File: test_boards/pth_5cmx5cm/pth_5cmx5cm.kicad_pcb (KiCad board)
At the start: 2 copper layers, 49.5 x 49.5 mm, 4 parts, among them Q1 BC560, Q2 2N3904

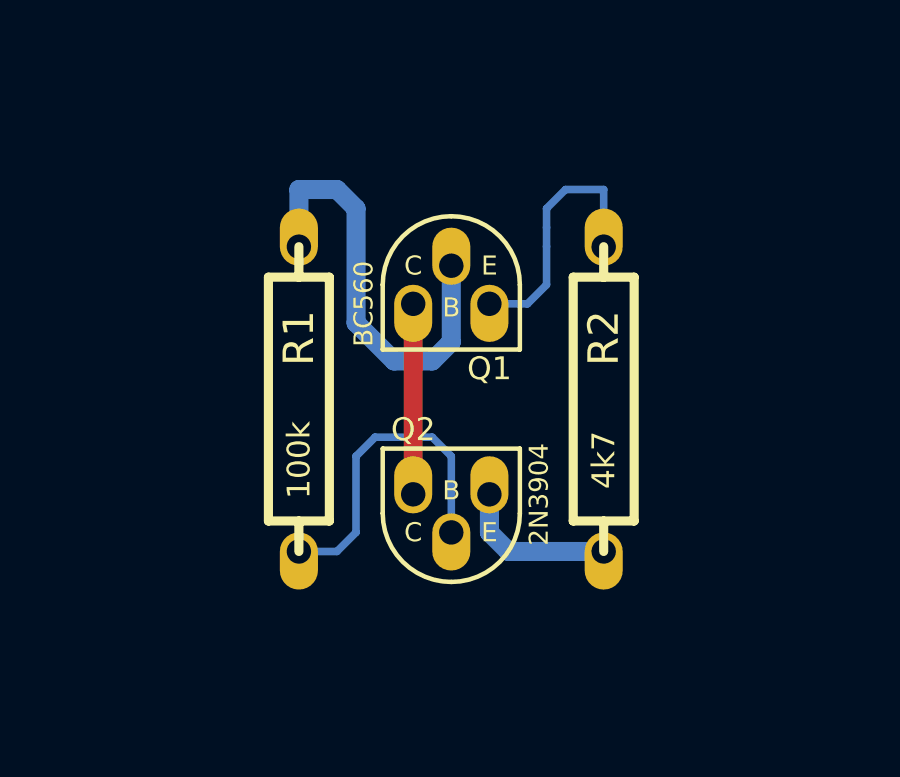
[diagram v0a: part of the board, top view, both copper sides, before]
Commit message: updating test board.
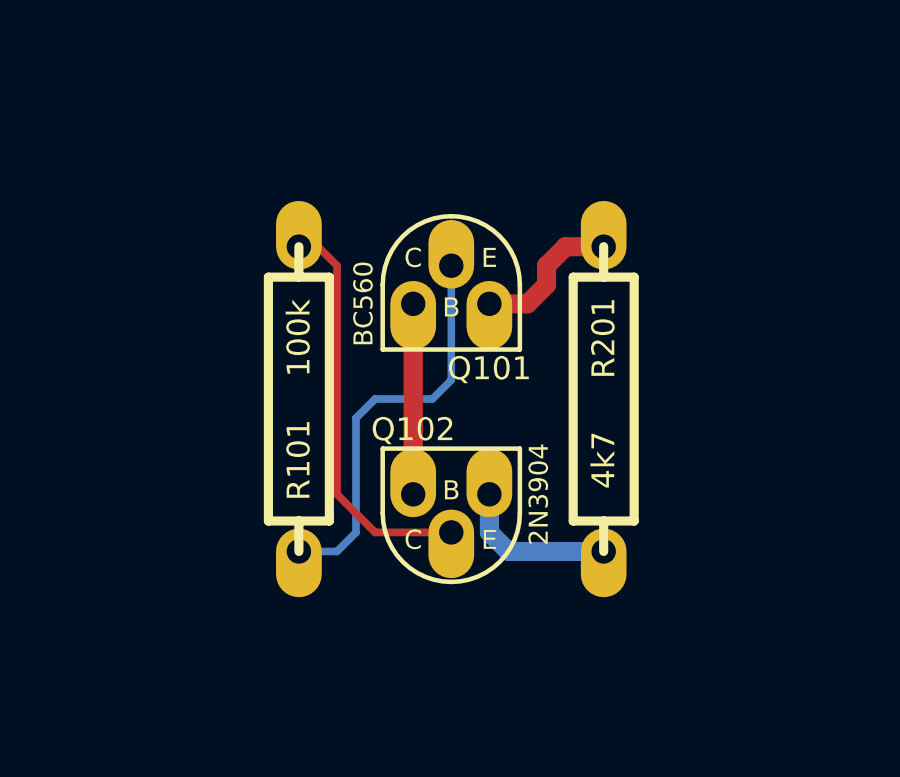
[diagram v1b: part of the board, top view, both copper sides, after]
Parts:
- removed Q1: BC560, TO-92_CBE
- removed Q2: 2N3904, TO-92_EBC
- removed R1: 100k, R_AXIAL_0W25
- removed R2: 4k7, R_AXIAL_0W25
- added Q101: BC560, TO-92_Q_CBE, F.Cu at (215.3, 118.7)
- added Q102: 2N3904, TO-92_Q_EBC, F.Cu at (215.3, 126.4)
- added R101: 100k, R_AXIAL_0W25, F.Cu at (210.2, 122.6)
- added R201: 4k7, R_AXIAL_0W25, F.Cu at (220.3, 122.6)
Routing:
- net N-000001: track 14.4 -> 4.97 mm
- net N-000002: track 5.34 -> 13.5 mm
- net N-000004: track 6.35 -> 13.5 mm
- net N-000005: track 10.9 -> 5.34 mm
- net N-000003: track 8.78 -> 6.35 mm

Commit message: adding mounting hole footprint, updating test board.
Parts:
- added H101: HOLE, hole_M3, F.Cu at (200.0, 111.1)
- added H102: HOLE, hole_M3, F.Cu at (243.2, 111.1)
- added H103: HOLE, hole_M3, F.Cu at (200.0, 154.3)
- added H104: HOLE, hole_M3, F.Cu at (243.2, 154.3)
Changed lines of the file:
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@@
     (tracks 21)
     (zones 0)
-    (modules 4)
+    (modules 8)
     (nets 6)
   )
@@
   )
   (net 0 "")
-  (net 1 N-000001)
-  (net 2 N-000002)
-  (net 3 N-000003)
-  (net 4 N-000004)
-  (net 5 N-000005)
+  (net 1 N-000005)
+  (net 2 N-000006)
+  (net 3 N-000007)
+  (net 4 N-000008)
+  (net 5 N-000009)
   (net_class Default "This is the default net class."
     (clearance 0.254)
@@
     (uvia_drill 0.127)
     (add_net "")
-    (add_net N-000001)
-    (add_net N-000002)
-    (add_net N-000003)
-    (add_net N-000004)
     (add_net N-000005)
+    (add_net N-000006)
+    (add_net N-000007)
+    (add_net N-000008)
+    (add_net N-000009)
   )
   (module TO-92_Q_EBC (layer F.Cu)
@@
     (pad 1 thru_hole oval (at 1.27 -0.635) (size 1.524 2.286) (drill 0.8128 (offset 0 -0.381))
       (layers *.Cu *.Mask F.SilkS)
-      (net 5 N-000005)
+      (net 4 N-000008)
     )
     (pad 2 thru_hole oval (at 0 0.635) (size 1.524 2.286) (drill 0.8128 (offset 0 0.381))
       (layers *.Cu *.Mask F.SilkS)
-      (net 4 N-000004)
+      (net 3 N-000007)
     )
     (pad 3 thru_hole oval (at -1.27 -0.635) (size 1.524 2.286) (drill 0.8128 (offset 0 -0.381))
       (layers *.Cu *.Mask F.SilkS)
-      (net 3 N-000003)
+      (net 2 N-000006)
     )
     (model to-xxx-packages/to92.wrl
@@
     (pad 1 thru_hole oval (at 1.27 -0.635 180) (size 1.524 2.286) (drill 0.8128 (offset 0 -0.381))
       (layers *.Cu *.Mask F.SilkS)
-      (net 3 N-000003)
+      (net 2 N-000006)
     )
     (pad 2 thru_hole oval (at 0 0.635 180) (size 1.524 2.286) (drill 0.8128 (offset 0 0.381))
       (layers *.Cu *.Mask F.SilkS)
-      (net 2 N-000002)
+      (net 1 N-000005)
     )
     (pad 3 thru_hole oval (at -1.27 -0.635 180) (size 1.524 2.286) (drill 0.8128 (offset 0 -0.381))
       (layers *.Cu *.Mask F.SilkS)
-      (net 1 N-000001)
+      (net 5 N-000009)
     )
     (model to-xxx-packages/to92.wrl
@@
     (pad 1 thru_hole oval (at -5.08 0 90) (size 2.286 1.524) (drill 0.8128 (offset -0.381 0))
       (layers *.Cu *.Mask F.SilkS)
-      (net 2 N-000002)
+      (net 1 N-000005)
     )
     (pad 2 thru_hole oval (at 5.08 0 90) (size 2.286 1.524) (drill 0.8128 (offset 0.381 0))
       (layers *.Cu *.Mask F.SilkS)
-      (net 4 N-000004)
+      (net 3 N-000007)
     )
     (model discret/resistor.wrl
@@
     (pad 1 thru_hole oval (at -5.08 0 270) (size 2.286 1.524) (drill 0.8128 (offset -0.381 0))
       (layers *.Cu *.Mask F.SilkS)
-      (net 1 N-000001)
+      (net 5 N-000009)
     )
     (pad 2 thru_hole oval (at 5.08 0 270) (size 2.286 1.524) (drill 0.8128 (offset 0.381 0))
       (layers *.Cu *.Mask F.SilkS)
-      (net 5 N-000005)
+      (net 4 N-000008)
     )
     (model discret/resistor.wrl
@@
     )
   )
+  (module hole_M3 (layer F.Cu)
+    (at 200.025 111.125)
+    (descr "M3 mounting hole")
+    (fp_text reference H101 (at 0 -3.048) (layer F.SilkS) hide
+      (effects (font (size 1.016 1.016) (thickness 0.254)))
+    )
+    (fp_text value HOLE (at 0 2.794) (layer F.SilkS) hide
+      (effects (font (size 1.016 1.016) (thickness 0.254)))
+    )
+    (fp_circle (center 0 0) (end 0 3.2) (layer F.SilkS) (width 0.15))
+    (pad 1 thru_hole circle (at 0 0) (size 6 6) (drill 3.2)
+      (layers *.Cu *.Mask F.SilkS)
+    )
+  )
+  (module hole_M3 (layer F.Cu)
+    (at 243.205 111.125)
+    (descr "M3 mounting hole")
+    (fp_text reference H102 (at 0 -3.048) (layer F.SilkS) hide
+      (effects (font (size 1.016 1.016) (thickness 0.254)))
+    )
+    (fp_text value HOLE (at 0 2.794) (layer F.SilkS) hide
+      (effects (font (size 1.016 1.016) (thickness 0.254)))
+    )
+    (fp_circle (center 0 0) (end 0 3.2) (layer F.SilkS) (width 0.15))
+    (pad 1 thru_hole circle (at 0 0) (size 6 6) (drill 3.2)
+      (layers *.Cu *.Mask F.SilkS)
+    )
+  )
+  (module hole_M3 (layer F.Cu)
+    (at 200.025 154.305)
+    (descr "M3 mounting hole")
+    (fp_text reference H103 (at 0 -3.048) (layer F.SilkS) hide
+      (effects (font (size 1.016 1.016) (thickness 0.254)))
+    )
+    (fp_text value HOLE (at 0 2.794) (layer F.SilkS) hide
+      (effects (font (size 1.016 1.016) (thickness 0.254)))
+    )
+    (fp_circle (center 0 0) (end 0 3.2) (layer F.SilkS) (width 0.15))
+    (pad 1 thru_hole circle (at 0 0) (size 6 6) (drill 3.2)
+      (layers *.Cu *.Mask F.SilkS)
+    )
+  )
+  (module hole_M3 (layer F.Cu)
+    (at 243.205 154.305)
+    (descr "M3 mounting hole")
+    (fp_text reference H104 (at 0 -3.048) (layer F.SilkS) hide
+      (effects (font (size 1.016 1.016) (thickness 0.254)))
+    )
+    (fp_text value HOLE (at 0 2.794) (layer F.SilkS) hide
+      (effects (font (size 1.016 1.016) (thickness 0.254)))
+    )
+    (fp_circle (center 0 0) (end 0 3.2) (layer F.SilkS) (width 0.15))
+    (pad 1 thru_hole circle (at 0 0) (size 6 6) (drill 3.2)
+      (layers *.Cu *.Mask F.SilkS)
+    )
+  )
   (gr_line (start 196.85 107.95) (end 196.85 157.48) (angle 90) (layer Edge.Cuts) (width 0.1))
   (gr_line (start 246.38 107.95) (end 196.85 107.95) (angle 90) (layer Edge.Cuts) (width 0.1))
   (gr_line (start 246.38 157.48) (end 246.38 107.95) (angle 90) (layer Edge.Cuts) (width 0.1))
   (gr_line (start 196.85 157.48) (end 246.38 157.48) (angle 90) (layer Edge.Cuts) (width 0.1))
-  (segment (start 216.535 119.38) (end 217.805 119.38) (width 0.635) (layer F.Cu) (net 1) (status 400000))
-  (segment (start 219.075 117.475) (end 220.345 117.475) (width 0.635) (layer F.Cu) (net 1) (status 800000))
-  (segment (start 218.44 118.11) (end 219.075 117.475) (width 0.635) (layer F.Cu) (net 1))
-  (segment (start 218.44 118.745) (end 218.44 118.11) (width 0.635) (layer F.Cu) (net 1))
-  (segment (start 217.805 119.38) (end 218.44 118.745) (width 0.635) (layer F.Cu) (net 1))
-  (segment (start 215.265 118.11) (end 215.265 121.92) (width 0.254) (layer B.Cu) (net 2) (status 400000))
-  (segment (start 211.455 127.635) (end 210.185 127.635) (width 0.254) (layer B.Cu) (net 2) (status 800000))
-  (segment (start 212.09 127) (end 211.455 127.635) (width 0.254) (layer B.Cu) (net 2))
-  (segment (start 212.09 123.19) (end 212.09 127) (width 0.254) (layer B.Cu) (net 2))
-  (segment (start 212.725 122.555) (end 212.09 123.19) (width 0.254) (layer B.Cu) (net 2))
-  (segment (start 214.63 122.555) (end 212.725 122.555) (width 0.254) (layer B.Cu) (net 2))
-  (segment (start 215.265 121.92) (end 214.63 122.555) (width 0.254) (layer B.Cu) (net 2))
-  (segment (start 213.995 119.38) (end 213.995 125.73) (width 0.635) (layer F.Cu) (net 3))
-  (segment (start 210.185 117.475) (end 210.82 117.475) (width 0.254) (layer F.Cu) (net 4) (status C00000))
-  (segment (start 212.725 127) (end 215.265 127) (width 0.254) (layer F.Cu) (net 4) (status 800000))
-  (segment (start 211.455 125.73) (end 212.725 127) (width 0.254) (layer F.Cu) (net 4))
-  (segment (start 211.455 118.11) (end 211.455 125.73) (width 0.254) (layer F.Cu) (net 4))
-  (segment (start 210.82 117.475) (end 211.455 118.11) (width 0.254) (layer F.Cu) (net 4) (status 400000))
-  (segment (start 217.17 127.635) (end 220.345 127.635) (width 0.635) (layer B.Cu) (net 5))
-  (segment (start 216.535 127) (end 217.17 127.635) (width 0.635) (layer B.Cu) (net 5))
-  (segment (start 216.535 125.73) (end 216.535 127) (width 0.635) (layer B.Cu) (net 5))
+  (segment (start 215.265 118.11) (end 215.265 121.92) (width 0.254) (layer B.Cu) (net 1))
+  (segment (start 211.455 127.635) (end 210.185 127.635) (width 0.254) (layer B.Cu) (net 1))
+  (segment (start 212.09 127) (end 211.455 127.635) (width 0.254) (layer B.Cu) (net 1))
+  (segment (start 212.09 123.19) (end 212.09 127) (width 0.254) (layer B.Cu) (net 1))
+  (segment (start 212.725 122.555) (end 212.09 123.19) (width 0.254) (layer B.Cu) (net 1))
+  (segment (start 214.63 122.555) (end 212.725 122.555) (width 0.254) (layer B.Cu) (net 1))
+  (segment (start 215.265 121.92) (end 214.63 122.555) (width 0.254) (layer B.Cu) (net 1))
+  (segment (start 213.995 119.38) (end 213.995 125.73) (width 0.635) (layer F.Cu) (net 2))
+  (segment (start 210.185 117.475) (end 210.82 117.475) (width 0.254) (layer F.Cu) (net 3))
+  (segment (start 212.725 127) (end 215.265 127) (width 0.254) (layer F.Cu) (net 3))
+  (segment (start 211.455 125.73) (end 212.725 127) (width 0.254) (layer F.Cu) (net 3))
+  (segment (start 211.455 118.11) (end 211.455 125.73) (width 0.254) (layer F.Cu) (net 3))
+  (segment (start 210.82 117.475) (end 211.455 118.11) (width 0.254) (layer F.Cu) (net 3))
+  (segment (start 217.17 127.635) (end 220.345 127.635) (width 0.635) (layer B.Cu) (net 4))
+  (segment (start 216.535 127) (end 217.17 127.635) (width 0.635) (layer B.Cu) (net 4))
+  (segment (start 216.535 125.73) (end 216.535 127) (width 0.635) (layer B.Cu) (net 4))
+  (segment (start 216.535 119.38) (end 217.805 119.38) (width 0.635) (layer F.Cu) (net 5))
+  (segment (start 219.075 117.475) (end 220.345 117.475) (width 0.635) (layer F.Cu) (net 5))
+  (segment (start 218.44 118.11) (end 219.075 117.475) (width 0.635) (layer F.Cu) (net 5))
+  (segment (start 218.44 118.745) (end 218.44 118.11) (width 0.635) (layer F.Cu) (net 5))
+  (segment (start 217.805 119.38) (end 218.44 118.745) (width 0.635) (layer F.Cu) (net 5))
 )

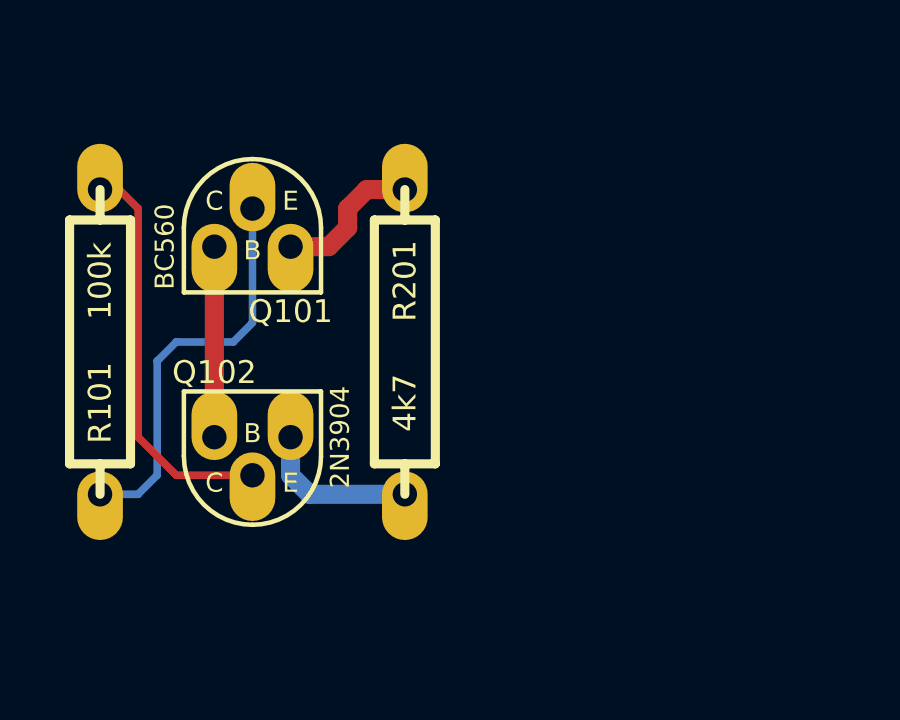
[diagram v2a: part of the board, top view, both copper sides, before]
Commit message: updating test board (trying out tweaked pad settings)
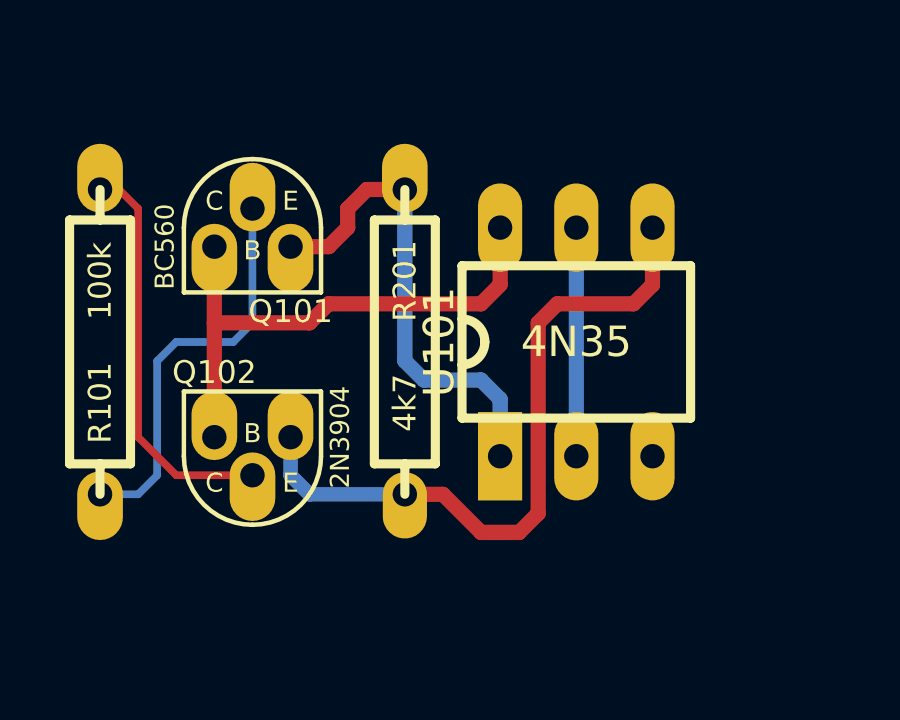
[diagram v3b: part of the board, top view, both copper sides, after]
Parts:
- added U101: 4N35, DIP6, F.Cu at (226.1, 122.6)
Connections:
- net N-000008 renamed GND
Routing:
- net GND: track 5.34 -> 23.2 mm
- net N-000002: track 6.35 -> 18.3 mm
- net N-000006: track 4.97 -> 16.3 mm
- net N-000001: track 0.00 -> 7.62 mm
